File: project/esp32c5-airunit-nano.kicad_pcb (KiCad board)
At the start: 2 copper layers, 19.1 x 21.8 mm, 26 parts, among them J1 FPC0.5B-WTX-24P, J2 Conn_01x01_Pin, J4 Conn_01x01_Pin, J5 Conn_01x01_Pin, J6 Conn_01x01_Pin, J7 Conn_01x01_Pin, J8 0475710001, J9 Conn_01x01_Pin, SW1 record, U1 MT3406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

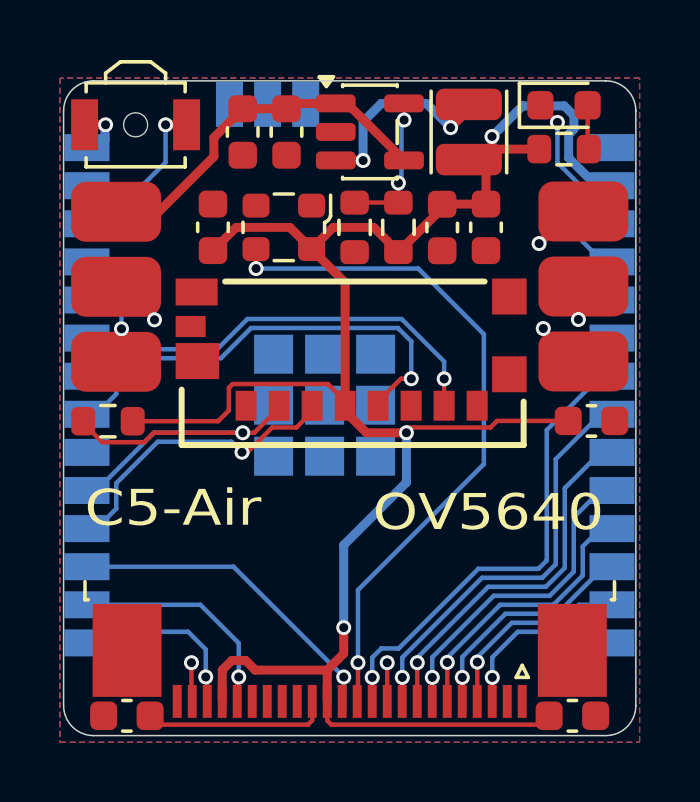
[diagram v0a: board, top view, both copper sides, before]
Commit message: i've updated the schematic and changed the button for a cheaper one
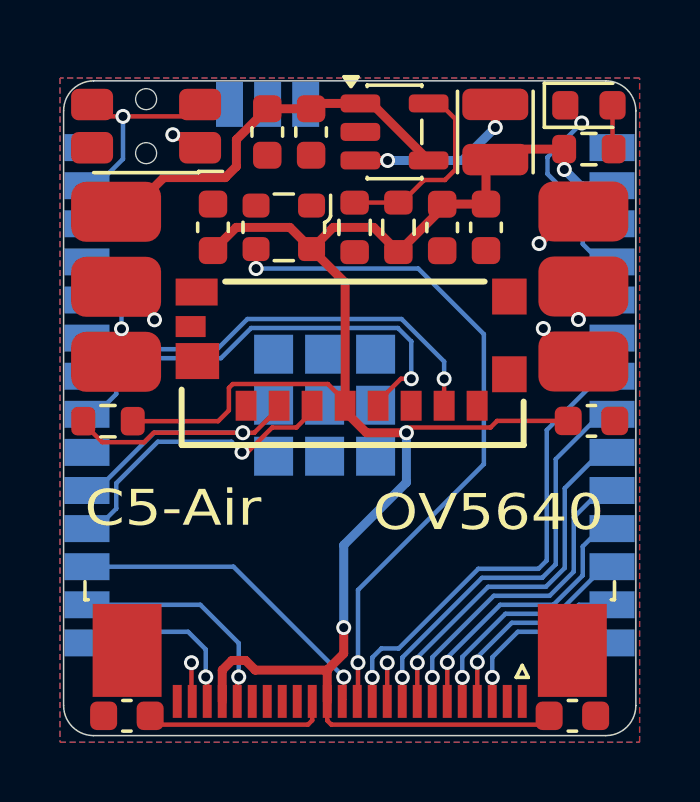
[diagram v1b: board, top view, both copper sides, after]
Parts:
- C1, C6: value 100nF -> 100nF 10V
- C2, C3, C4, C5, C7, C8: value 10uF -> 10uF 10V
- J8: value 0475710001 -> TF-021B-H265
- SW1: value record -> EVQP7C01P; footprint Button_Switch_SMD:SW_SPST_B3U-3000P-B -> Button_Switch_SMD:SW_SPST_EVQP7C
- U2: value ESP32-C5-WROOM-1U -> ESP32-C5-WROOM-1U-N8R8
- moved L1 0.88 mm to (154.2, 72.0)
- moved D1 0.83 mm to (157.4, 71.2)
- moved R3 0.83 mm to (157.4, 72.6)
- moved C1 0.82 mm to (146.6, 72.0)
- moved C2 0.82 mm to (148.1, 72.0)
- moved U1 0.82 mm to (150.9, 72.0)
- moved SW1 0.35 mm to (142.6, 71.8), turned to 180 degrees
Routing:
- net +3V0: track 68.7 -> 62.9 mm
- net record: track 4.89 -> 6.92 mm
- net Net-(U1-VOUT): track 4.85 -> 6.60 mm, vias 2 -> 0
- net Net-(U1-SW): track 6.74 -> 5.72 mm
- net VCC: track 12.3 -> 13.2 mm
- net GND: track 6.43 -> 5.60 mm
- net led: track 6.38 -> 7.03 mm

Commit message: Add files via upload
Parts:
- D1: value red -> NCD0603R2
- R2: value tbd -> 25kR
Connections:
- Y1 pad 1: unconnected-(Y1-Tri-State-Pad1) -> +3V0
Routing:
- net +3V0: track 62.9 -> 64.3 mm
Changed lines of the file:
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@@
 			(layers "F.Cu" "F.Mask" "F.Paste")
 			(roundrect_rratio 0.25)
-			(net "unconnected-(Y1-Tri-State-Pad1)")
+			(net "+3V0")
 			(pinfunction "Tri-State_1")
-			(pintype "input+no_connect")
+			(pintype "input")
 		)
 		(pad "2" smd roundrect
@@
 			)
 		)
-		(property "Value" "tbd"
+		(property "Value" "25kR"
 			(at 0 1.43 90)
 			(layer "F.Fab")
@@
 			)
 		)
-		(property "Value" "red"
+		(property "Value" "NCD0603R2"
 			(at 0 1.43 0)
 			(layer "F.Fab")
@@
 		(width 0.3)
 		(layer "F.Cu")
+		(net "+3V0")
+	)
+	(segment
+		(start 148.115 74.4925)
+		(end 148.115 75.9425)
+		(width 0.3)
+		(layer "F.Cu")

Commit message: i've updated the files
there were some major errors in the v1.0 of the project
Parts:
- R1, R6: value 100kR -> 47kR
- R2: value 25kR -> 12kR
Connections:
- J1 pad 17: unconnected-(J1-Pin_17-Pad17) -> GND
- U2 pad 10: d4 -> d3
- U2 pad 11: d0 -> d1
- U2 pad 12: d3 -> d2
- U2 pad 13: d1 -> uart1_rx
- U2 pad 14: d2 -> uart1_tx
- U2 pad 15: sda -> record
- U2 pad 16: scl -> sda
- U2 pad 17: d7 -> scl
- U2 pad 18: sd_cmd -> led
- U2 pad 19: sd_cd -> unconnected-(U2-GPIO15-Pad19)
- U2 pad 21: sd_clk -> sd_cd
- U2 pad 23: sd_data -> sd_cmd
- U2 pad 26: unconnected-(U2-GPIO25-Pad26) -> sd_clk
- U2 pad 27: record -> sd_data
- U2 pad 3: unconnected-(U2-EN/CHIP_PU-Pad3) -> +3V0
- U2 pad 4: led -> d7
- U2 pad 5: uart1_tx -> d6
- U2 pad 6: uart1_rx -> d5
- U2 pad 7: d6 -> pclk
- U2 pad 8: d5 -> d4
- U2 pad 9: pclk -> d0
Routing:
- net record: track 6.92 -> 34.6 mm
- net led: track 7.03 -> 24.5 mm, vias 1 -> 3
- net uart1_tx: track 3.19 -> 15.2 mm, vias 1 -> 3
- net d7: track 10.9 -> 18.6 mm
- net uart1_rx: track 4.62 -> 11.3 mm
- net +3V0: track 64.3 -> 67.8 mm, vias 3 -> 2
- net d2: track 5.97 -> 8.59 mm
- net d1: track 6.69 -> 9.11 mm
- net d3: track 7.72 -> 9.79 mm
- net uart0_rx: track 2.99 -> 4.80 mm
- net sd_data: track 14.5 -> 16.3 mm
- net sd_cd: track 13.4 -> 11.7 mm
- net d0: track 9.30 -> 10.8 mm
- net d4: track 10.8 -> 12.3 mm
- net pclk: track 12.3 -> 13.8 mm
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
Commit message: Add files via upload
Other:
- board text added: "version 1.1 vcc: 3.0v to 5.5v"
- board text removed: "version 1.0 vcc: 3.0v to 5.5v"
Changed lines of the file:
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@@
 	)
 	(paper "A4")
+	(title_block
+		(title "esp32c5-airunit-nano")
+		(date "2026-06-07")
+		(rev "v1.1")
+		(company "us3r_d0e5nt_3x1st")
+	)
 	(layers
 		(0 "F.Cu" signal)
@@
 		)
 	)
-	(gr_text "version 1.0\nvcc: 3.0v to 5.5v"
+	(gr_text "version 1.1\nvcc: 3.0v to 5.5v"
 		(at 149.24 87.39 0)
 		(layer "B.SilkS")

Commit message: i've uploaded the v1.2
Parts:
- removed C7: 10uF 10V, Capacitor_SMD:C_0603_1608Metric
- removed Y1: YD24MUBCE2O, Oscillator:Oscillator_SMD_ECS_2520MV-xxx-xx-4Pin_2.5x2.0mm
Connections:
- D1 pad 1: led -> record
- U2 pad 18: led -> xclk
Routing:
- net led: track 24.5 -> 0.00 mm, vias 3 -> 0
- net record: track 34.6 -> 47.2 mm, vias 1 -> 2
- net +3V0: track 67.8 -> 58.9 mm
- net xclk: track 24.0 -> 15.4 mm, vias 2 -> 3
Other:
- board text added: "version 1.2 vcc: 3.0v to 5.5v"
- board text removed: "version 1.1 vcc: 3.0v to 5.5v"

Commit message: Add files via upload
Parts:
- moved C8 12.9 mm to (146.3, 75.2), turned to 90 degrees
- moved R6 7.33 mm to (144.8, 75.2), turned to 90 degrees
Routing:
- net +3V0: track 58.9 -> 49.4 mm, vias 2 -> 1
- net sd_cd: track 11.7 -> 12.9 mm
- net sd_cmd: track 9.96 -> 9.45 mm
- net GND: vias 8 -> 9
